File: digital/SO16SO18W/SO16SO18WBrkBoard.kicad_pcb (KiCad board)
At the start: 2 copper layers, 22.6 x 23.9 mm, 4 parts, among them J1 CONN_01X09, J2 CONN_01X09, U1 MIC2981, U2 HEF4794B

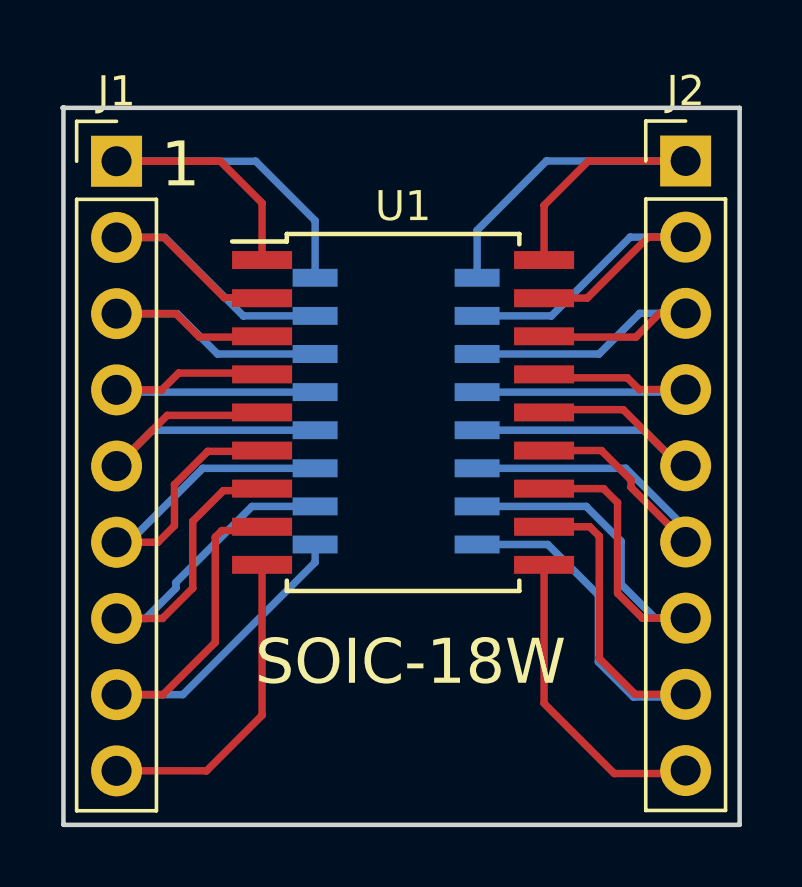
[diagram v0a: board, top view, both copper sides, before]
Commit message: SO16SO18W - fixed header spacing
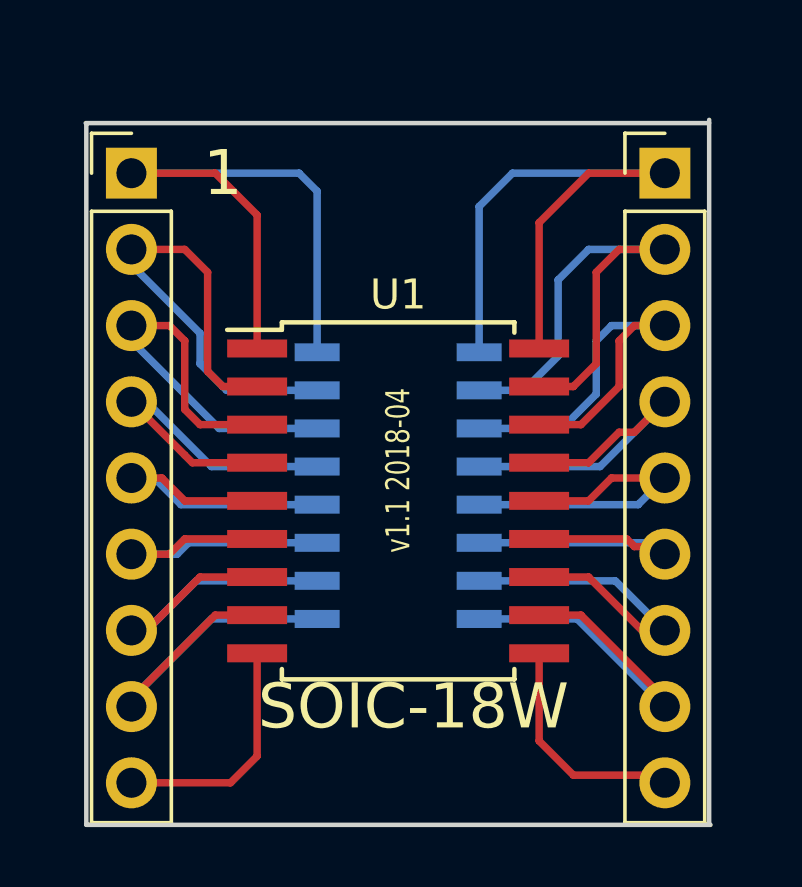
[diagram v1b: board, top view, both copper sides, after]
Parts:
- moved U1 2.95 mm to (148.3, 108.0)
- moved U2 2.48 mm to (148.3, 107.4)
- moved J2 0.81 mm to (157.2, 97.0)
- moved J1 0.64 mm to (139.4, 97.0)
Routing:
- net Net-(J2-Pad8): track 19.8 -> 13.0 mm
- net Net-(J2-Pad7): track 17.6 -> 11.8 mm
- net GND: track 18.3 -> 12.9 mm
- net Net-(J1-Pad7): track 16.3 -> 11.3 mm
- net Net-(J1-Pad1): track 16.7 -> 21.0 mm
- net Net-(J1-Pad6): track 14.6 -> 10.7 mm
- net Net-(J1-Pad2): track 13.4 -> 17.0 mm
- net Net-(J2-Pad6): track 14.4 -> 10.7 mm
- net Net-(J2-Pad9): track 11.0 -> 7.69 mm
- net Net-(J2-Pad1): track 17.3 -> 20.6 mm
- net Net-(J2-Pad2): track 14.3 -> 17.5 mm
- net Net-(J1-Pad9): track 10.6 -> 7.99 mm
- net Net-(J2-Pad5): track 13.5 -> 11.1 mm
- net Net-(J1-Pad3): track 12.4 -> 14.8 mm
- net Net-(J2-Pad3): track 13.3 -> 15.1 mm
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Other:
- board size 22.6 x 23.9 mm -> 20.8 x 23.5 mm
- board text added: "v1.1 2018-04"
